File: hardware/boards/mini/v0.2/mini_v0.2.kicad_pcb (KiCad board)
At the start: 8 copper layers, 20 x 41 mm, 100 parts, among them IC1 NAU88C22YG, IC3 IS42S16160J-6BLI, J2 Top, J3 Bottom, Q1 PMV37EN22, U1 W25Q128JVP, U2 LTV-217-G, U4 STM32H750XBHx, Y1 Crystal_GND24, Y3 32.768kHz

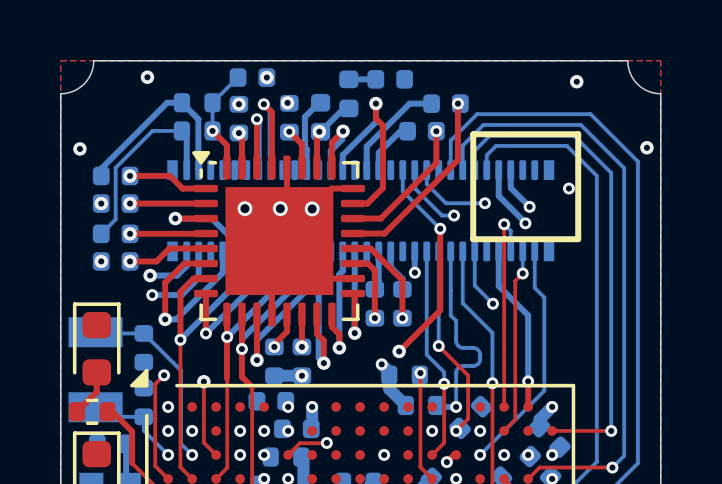
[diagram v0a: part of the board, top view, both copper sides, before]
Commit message: mini: resolve ERC errors
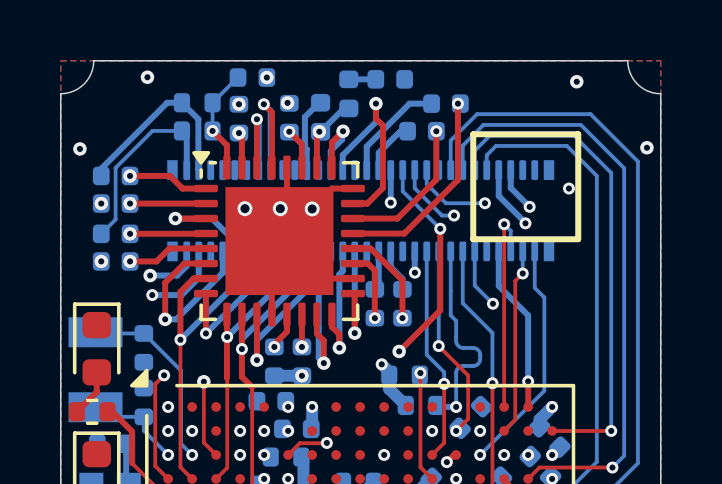
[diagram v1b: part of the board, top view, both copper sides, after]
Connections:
- J2 pad 25: unconnected-(J2-Pad25) -> /BOOT0
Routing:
- net /BOOT0: track 0.79 -> 12.6 mm, vias 1 -> 2
